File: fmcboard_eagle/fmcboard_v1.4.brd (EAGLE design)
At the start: 147 x 74 mm, 138 parts, among them IC1 OPA699ID, IC10 LTC6229IMS8E#TRPBF, IC11 7805TV, IC12 SN74AUC2G66DCTR, IC13 SN74AUC2G66DCTR, IC14 SN74AUC2G66DCTR, IC15 SN74AUC2G66DCTR, IC16 DAC7578SPWR, IC2 DAC7578SPWR, IC3 LTC6229IMS8E#TRPBF, IC4 LTC6229IMS8E#TRPBF, IC5 LM358, IC6 OPA699ID, IC7 OPA699ID, IC8 LTC6229IMS8E#TRPBF, IC9 LTC6229IMS8E#TRPBF, J1 8pin, J10 8pin, J12 4p-2.54, J2 ASP-134604-01, J3 4p-2.54, J4 4p-2.54, J5 8pin, J6 4p-2.54, J7 4p-2.54, J8 4p-2.54, J9 8pin, U1 TXS0108EPWR, U2 STMICROELECTRONICS_L7905ACVST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

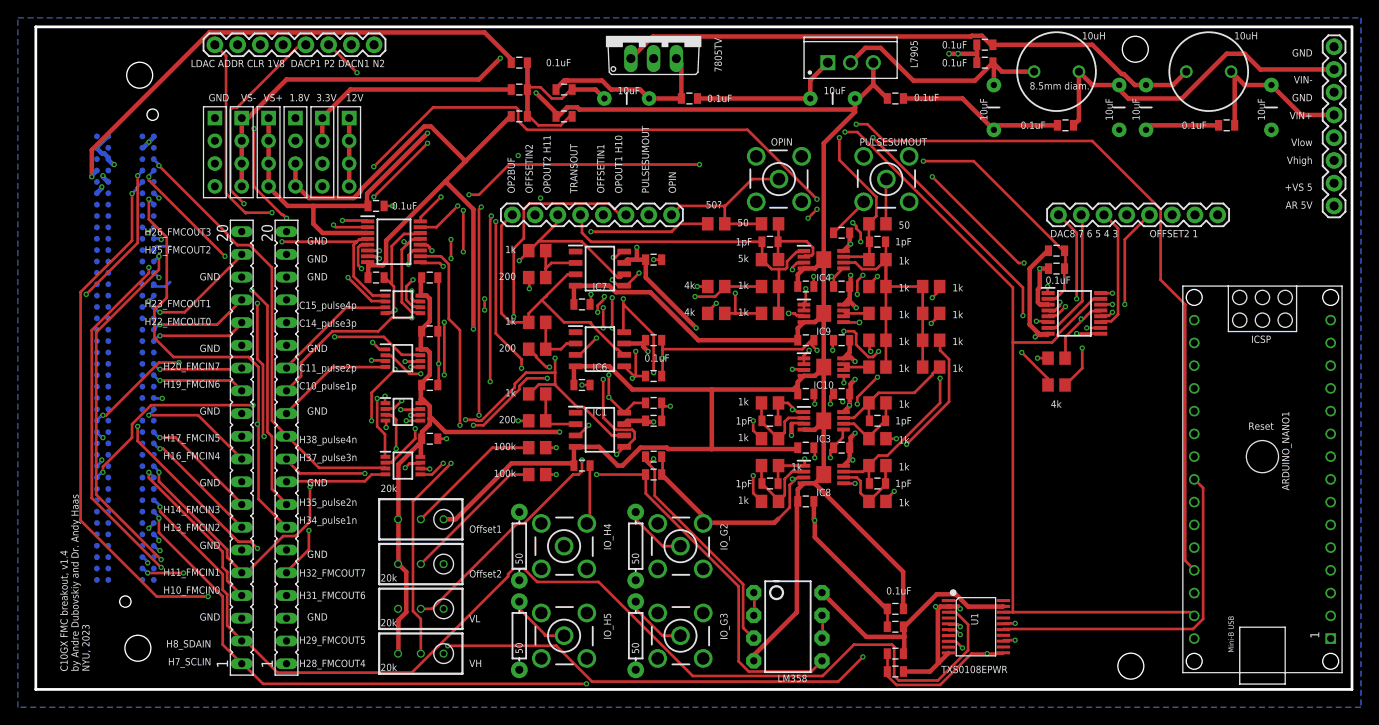
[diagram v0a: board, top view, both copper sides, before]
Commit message: v1.41 fix VS+ -> 1V8 for switches
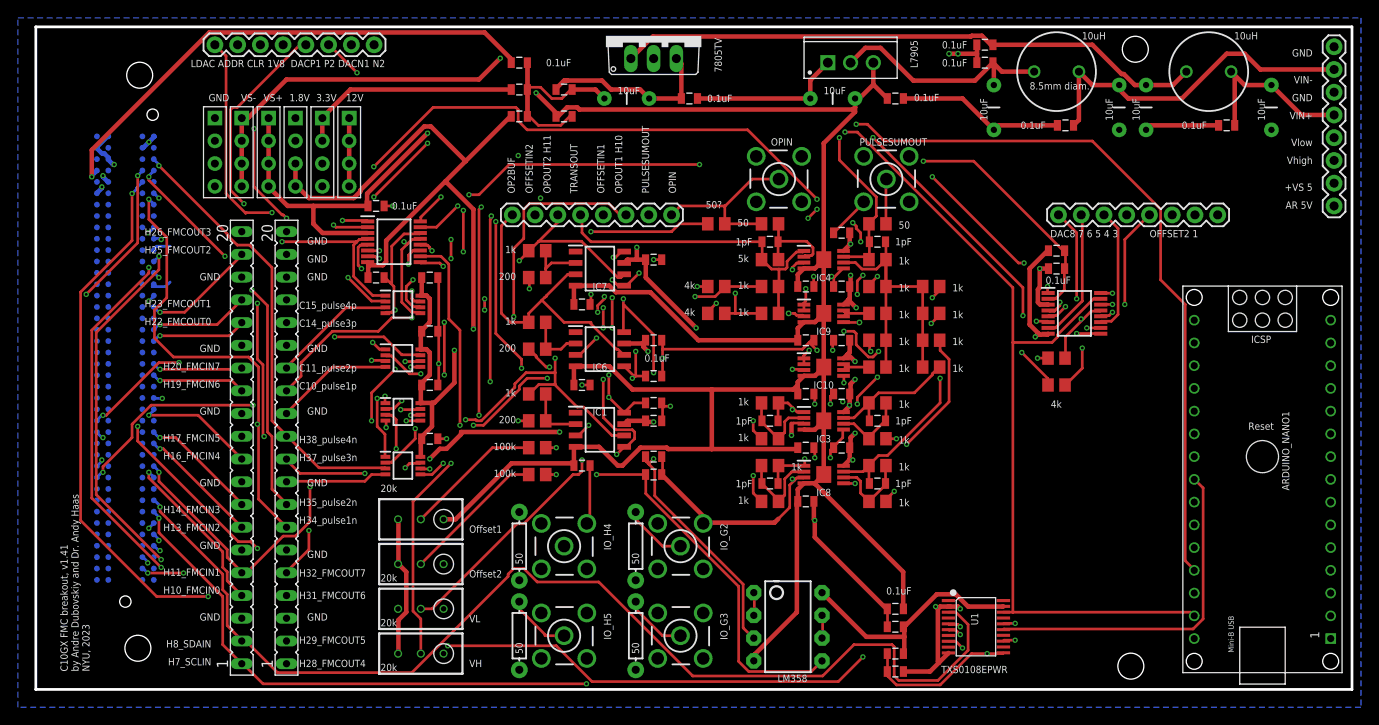
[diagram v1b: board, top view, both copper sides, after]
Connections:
- net 1V8: now also C50.1, C51.1, C52.1, C53.1, IC12.8, IC13.8, IC14.8, IC15.8
- net VS+: no longer C50.1, C51.1, C52.1, C53.1, IC12.8, IC13.8, IC14.8, IC15.8
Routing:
- net 1V8: track 240.9 -> 275.9 mm, vias 5 -> 6
- net VS+: track 409.6 -> 384.8 mm, vias 15 -> 16
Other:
- board text added: "C10GX FMC breakout, v1.41 by Andre Dubovskiy and Dr. Andy Haas NYU, 2023"
- board text removed: "C10GX FMC breakout, v1.4 by Andre Dubovskiy and Dr. Andy Haas NYU, 2023"
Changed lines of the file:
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@@
 <text x="71.5" y="55.4" size="0.8128" layer="21" rot="R90">OPIN</text>
 <text x="142.6" y="71.5" size="0.8128" layer="21" rot="R180">GND</text>
-<text x="6" y="2" size="0.8128" layer="21" rot="R90">C10GX FMC breakout, v1.4
+<text x="6" y="2" size="0.8128" layer="21" rot="R90">C10GX FMC breakout, v1.41
 by Andre Dubovskiy and Dr. Andy Haas
 NYU, 2023</text>
@@
 <wire x1="108" y1="4" x2="108.065" y2="4.09" width="0.3048" layer="1"/>
 <wire x1="95.125" y1="1.875" x2="95.1" y2="2" width="0.3048" layer="1"/>
-<wire x1="105" y1="70" x2="105.1" y2="70" width="0.3048" layer="1"/>
 <wire x1="105.125" y1="70.125" x2="105.125" y2="71" width="0.3048" layer="1"/>
 <wire x1="105.125" y1="71" x2="105.125" y2="72" width="0.3048" layer="1"/>
@@
 <via x="111.625" y="39.375" extent="1-16" drill="0.3048"/>
 <via x="103.25" y="9" extent="1-16" drill="0.3048"/>
+<contactref element="C52" pad="1"/>
+<contactref element="C53" pad="1"/>
+<contactref element="C50" pad="1"/>
+<contactref element="C51" pad="1"/>
+<contactref element="IC12" pad="8"/>
+<wire x1="43.625" y1="44" x2="43.25" y2="44" width="0.508" layer="1"/>
+<wire x1="44" y1="43.625" x2="43.625" y2="44" width="0.508" layer="1"/>
+<wire x1="44" y1="41" x2="44" y2="43.625" width="0.508" layer="1"/>
+<wire x1="43.25" y1="44" x2="42.95" y2="43.975" width="0.508" layer="1"/>
+<contactref element="IC13" pad="8"/>
+<wire x1="43" y1="40" x2="43" y2="38" width="0.508" layer="1"/>
+<wire x1="43" y1="38" x2="42.95" y2="37.975" width="0.508" layer="1"/>
+<wire x1="43.625" y1="38" x2="43.25" y2="38" width="0.508" layer="1"/>
+<wire x1="44" y1="37.625" x2="43.625" y2="38" width="0.508" layer="1"/>
+<wire x1="44" y1="35.125" x2="44" y2="37.625" width="0.508" layer="1"/>
+<wire x1="43.125" y1="34.25" x2="44" y2="35.125" width="0.508" layer="1"/>
+<wire x1="43.25" y1="38" x2="42.95" y2="37.975" width="0.508" layer="1"/>
+<contactref element="IC14" pad="8"/>
+<contactref element="IC15" pad="8"/>
+<wire x1="44" y1="41" x2="43" y2="40" width="0.508" layer="1"/>
+<wire x1="43" y1="28" x2="43" y2="26" width="0.508" layer="1"/>
+<wire x1="43" y1="26" x2="42.95" y2="25.975" width="0.508" layer="1"/>
+<wire x1="43" y1="28" x2="43.1" y2="28" width="0.508" layer="1"/>
+<wire x1="43.1" y1="40" x2="43" y2="40" width="0.508" layer="1"/>
+<wire x1="43" y1="34" x2="43" y2="32" width="0.508" layer="1"/>
+<wire x1="43" y1="32" x2="42.95" y2="31.975" width="0.508" layer="1"/>
+<wire x1="43" y1="34" x2="43.1" y2="34" width="0.508" layer="1"/>
+<wire x1="43.125" y1="34.25" x2="43.1" y2="34" width="0.508" layer="1"/>
+<wire x1="44.25" y1="29.375" x2="43.125" y2="28.25" width="0.508" layer="1"/>
+<wire x1="44.25" y1="32" x2="44.25" y2="29.375" width="0.508" layer="1"/>
+<wire x1="43.25" y1="32" x2="44.25" y2="32" width="0.508" layer="1"/>
+<wire x1="43.125" y1="28.25" x2="43.1" y2="28" width="0.508" layer="1"/>
+<wire x1="43.25" y1="32" x2="42.95" y2="31.975" width="0.508" layer="1"/>
+<wire x1="46.75" y1="34.25" x2="44.5" y2="32" width="0.508" layer="1"/>
+<wire x1="46.75" y1="37.875" x2="46.75" y2="34.25" width="0.508" layer="1"/>
+<wire x1="48.875" y1="40" x2="46.75" y2="37.875" width="0.508" layer="15"/>
+<wire x1="44.5" y1="32" x2="44.25" y2="32" width="0.508" layer="1"/>
+<wire x1="48.875" y1="40" x2="48.875" y2="40.25" width="0.508" layer="15"/>
+<via x="46.75" y="37.875" extent="1-16" drill="0.3048"/>
+<wire x1="43.1" y1="46" x2="43.1" y2="44.15" width="0.508" layer="1"/>
+<wire x1="43.1" y1="44.15" x2="43.25" y2="44" width="0.508" layer="1"/>
 </signal>
 <signal name="3V3" class="1">
@@
 <wire x1="145" y1="56.5" x2="145" y2="56.54" width="0.508" layer="15"/>
 <wire x1="91" y1="50" x2="91" y2="49.75" width="0.508" layer="15"/>
-<wire x1="58.5" y1="28.75" x2="45.75" y2="28.75" width="0.508" layer="1"/>
+<wire x1="58.5" y1="28.75" x2="47.5" y2="28.75" width="0.508" layer="1"/>
 <wire x1="67.625" y1="28.75" x2="58.5" y2="28.75" width="0.508" layer="15"/>
 <wire x1="68.75" y1="29.875" x2="67.625" y2="28.75" width="0.508" layer="15"/>
@@
 <contactref element="IC2" pad="3"/>
 <contactref element="C48" pad="1"/>
-<contactref element="C52" pad="1"/>
-<contactref element="C53" pad="1"/>
-<contactref element="C50" pad="1"/>
-<contactref element="C51" pad="1"/>
-<contactref element="IC12" pad="8"/>
-<contactref element="IC13" pad="8"/>
-<contactref element="IC14" pad="8"/>
-<contactref element="IC15" pad="8"/>
 <wire x1="28.125" y1="54" x2="31" y2="54" width="0.508" layer="1"/>
 <wire x1="31" y1="54" x2="37.1" y2="54" width="0.508" layer="1"/>
@@
 <wire x1="40.5" y1="19" x2="40.46" y2="19" width="0.508" layer="1"/>
 <wire x1="40.5" y1="14.25" x2="40.46" y2="14" width="0.508" layer="1"/>
-<wire x1="43" y1="46" x2="43" y2="44" width="0.508" layer="1"/>
-<wire x1="43" y1="44" x2="42.95" y2="43.975" width="0.508" layer="1"/>
-<wire x1="43" y1="46" x2="43.1" y2="46" width="0.508" layer="1"/>
-<wire x1="43" y1="40" x2="43" y2="38" width="0.508" layer="1"/>
-<wire x1="43" y1="38" x2="42.95" y2="37.975" width="0.508" layer="1"/>
-<wire x1="43" y1="40" x2="43.1" y2="40" width="0.508" layer="1"/>
-<wire x1="43" y1="28" x2="43" y2="27.375" width="0.508" layer="1"/>
-<wire x1="43" y1="27.375" x2="43" y2="26" width="0.508" layer="1"/>
-<wire x1="43" y1="26" x2="42.95" y2="25.975" width="0.508" layer="1"/>
-<wire x1="43" y1="28" x2="43.1" y2="28" width="0.508" layer="1"/>
-<wire x1="43" y1="34" x2="43" y2="32.375" width="0.508" layer="1"/>
-<wire x1="43" y1="32.375" x2="43" y2="32" width="0.508" layer="1"/>
-<wire x1="43" y1="32" x2="42.95" y2="31.975" width="0.508" layer="1"/>
-<wire x1="43" y1="34" x2="43.1" y2="34" width="0.508" layer="1"/>
-<wire x1="43.125" y1="28.75" x2="43.125" y2="28.25" width="0.508" layer="1"/>
-<wire x1="44" y1="29.625" x2="43.125" y2="28.75" width="0.508" layer="1"/>
-<wire x1="44" y1="31.625" x2="44" y2="30.25" width="0.508" layer="1"/>
-<wire x1="44" y1="30.25" x2="44" y2="29.625" width="0.508" layer="1"/>
-<wire x1="43.25" y1="32.375" x2="44" y2="31.625" width="0.508" layer="1"/>
-<wire x1="43.125" y1="28.25" x2="43.1" y2="28" width="0.508" layer="1"/>
-<wire x1="43.25" y1="32.375" x2="43" y2="32.375" width="0.508" layer="1"/>
-<wire x1="43.625" y1="38" x2="43.25" y2="38" width="0.508" layer="1"/>
-<wire x1="44" y1="37.625" x2="43.625" y2="38" width="0.508" layer="1"/>
-<wire x1="44" y1="35.125" x2="44" y2="37.625" width="0.508" layer="1"/>
-<wire x1="43.125" y1="34.25" x2="44" y2="35.125" width="0.508" layer="1"/>
-<wire x1="43.25" y1="38" x2="42.95" y2="37.975" width="0.508" layer="1"/>
-<wire x1="43.125" y1="34.25" x2="43.1" y2="34" width="0.508" layer="1"/>
-<wire x1="43.625" y1="44" x2="43.25" y2="44" width="0.508" layer="1"/>
-<wire x1="44" y1="43.625" x2="43.625" y2="44" width="0.508" layer="1"/>
-<wire x1="44" y1="41.125" x2="44" y2="43.625" width="0.508" layer="1"/>
-<wire x1="43.125" y1="40.25" x2="44" y2="41.125" width="0.508" layer="1"/>
-<wire x1="43.25" y1="44" x2="42.95" y2="43.975" width="0.508" layer="1"/>
-<wire x1="43.125" y1="40.25" x2="43.1" y2="40" width="0.508" layer="1"/>
-<wire x1="40.5" y1="25.125" x2="40.5" y2="19.25" width="0.508" layer="1"/>
-<wire x1="42.75" y1="27.375" x2="40.5" y2="25.125" width="0.508" layer="1"/>
-<wire x1="40.5" y1="19.25" x2="40.46" y2="19" width="0.508" layer="1"/>
-<wire x1="42.75" y1="27.375" x2="43" y2="27.375" width="0.508" layer="1"/>
-<wire x1="44.25" y1="30.25" x2="45.75" y2="28.75" width="0.508" layer="1"/>
-<wire x1="44.25" y1="30.25" x2="44" y2="30.25" width="0.508" layer="1"/>
 <via x="43.75" y="62.125" extent="1-16" drill="0.3048"/>
 <contactref element="IC16" pad="3"/>
@@
 <wire x1="112.125" y1="44.8752375" x2="112.125" y2="47" width="0.508" layer="1"/>
 <wire x1="111.9181" y1="43.2316625" x2="111.9181" y2="44.6683375" width="0.508" layer="1"/>
+<wire x1="40.5" y1="22.25" x2="40.5" y2="19" width="0.508" layer="15"/>
+<wire x1="44" y1="25.75" x2="40.5" y2="22.25" width="0.508" layer="15"/>
+<wire x1="45.125" y1="26.875" x2="44" y2="25.75" width="0.508" layer="1"/>
+<wire x1="45.875" y1="26.875" x2="45.125" y2="26.875" width="0.508" layer="1"/>
+<wire x1="47.5" y1="28.5" x2="45.875" y2="26.875" width="0.508" layer="1"/>
+<wire x1="40.5" y1="19" x2="40.46" y2="19" width="0.508" layer="15"/>
+<wire x1="47.5" y1="28.5" x2="47.5" y2="28.75" width="0.508" layer="1"/>
+<via x="44" y="25.75" extent="1-16" drill="0.3048"/>
 </signal>
 <signal name="VS-" class="1">

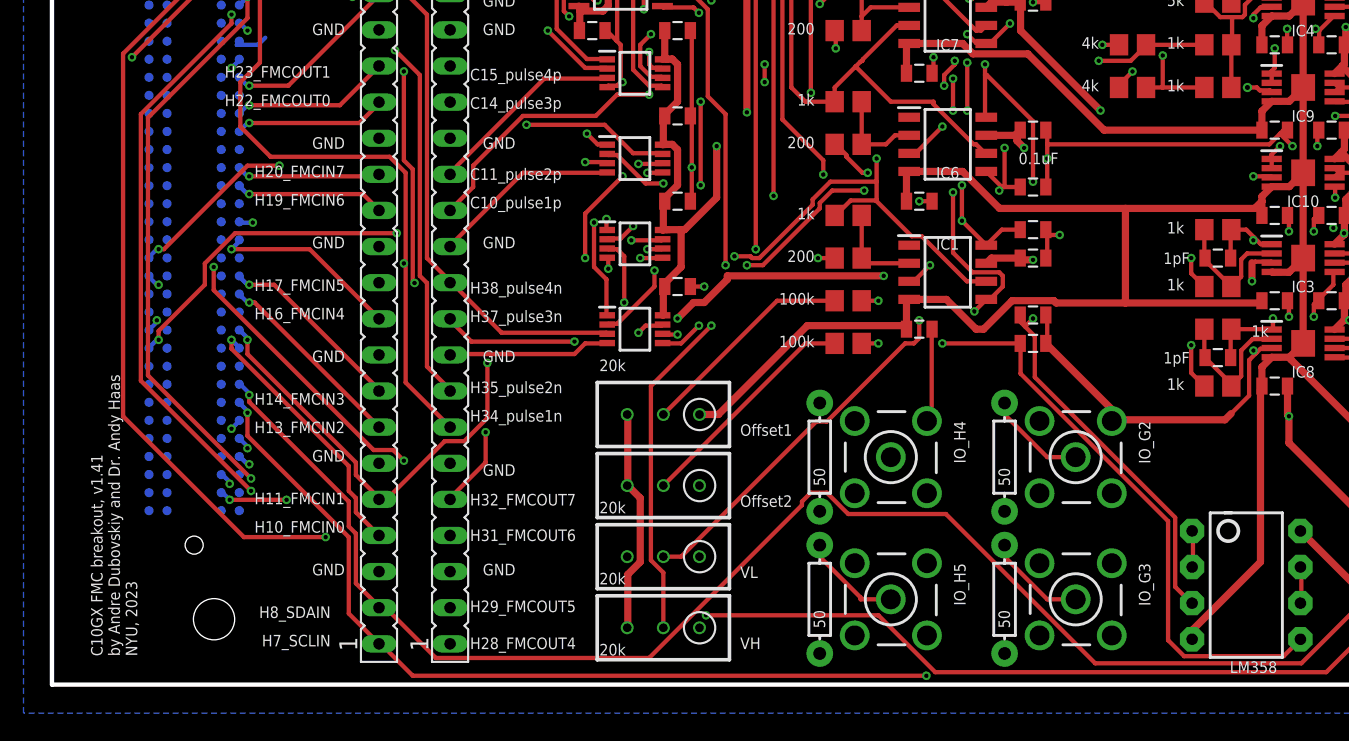
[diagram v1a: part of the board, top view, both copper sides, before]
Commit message: v1.42 add 100 Ohm resistors to GND for when switches are off (V should go to GND fast!)
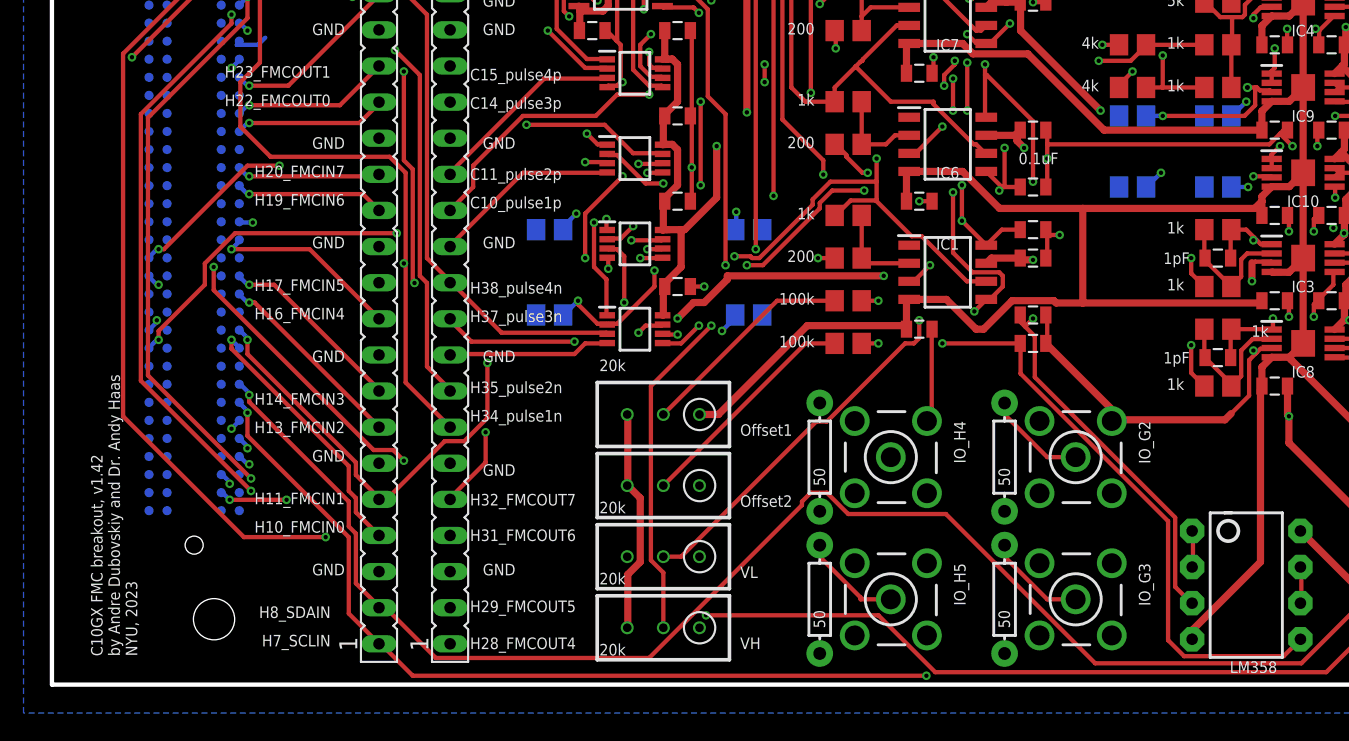
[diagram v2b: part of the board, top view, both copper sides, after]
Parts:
- added R37, R39, R41, R43, R44, R45, R46, R47: 100, rcl:R0805
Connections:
- net GND: now also R37.1, R39.2, R41.1, R43.2, R44.2, R45.2, R46.1, R47.1
- net PULSEINN1: now also R44.1
- net PULSEINN2: now also R47.2
- net PULSEINN3: now also R45.1
- net PULSEINN4: now also R46.2
- net PULSEINP1: now also R39.1
- net PULSEINP2: now also R37.2
- net PULSEINP3: now also R43.1
- net PULSEINP4: now also R41.2
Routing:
- net PULSEINP1: track 83.2 -> 92.4 mm, vias 6 -> 7
- net PULSEINN1: track 48.3 -> 54.6 mm, vias 2 -> 3
- net PULSEINN3: track 50.6 -> 54.9 mm, vias 2 -> 3
- net PULSEINP4: track 59.8 -> 61.9 mm, vias 2 -> 3
- net PULSEINN4: track 55.7 -> 57.5 mm, vias 2 -> 3
- net PULSEINN2: track 61.7 -> 63.5 mm, vias 2 -> 3
- net PULSEINP3: track 55.1 -> 56.6 mm, vias 4 -> 5
- net PULSEINP2: track 62.0 -> 63.4 mm, vias 2 -> 3
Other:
- board text added: "C10GX FMC breakout, v1.42 by Andre Dubovskiy and Dr. Andy Haas NYU, 2023"
- board text removed: "C10GX FMC breakout, v1.41 by Andre Dubovskiy and Dr. Andy Haas NYU, 2023"
